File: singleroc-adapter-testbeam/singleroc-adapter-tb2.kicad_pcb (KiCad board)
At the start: 2 copper layers, 64 x 52 mm, 28 parts, among them J1 CONN_40, J2 CONN-SCSI68, P1 CONN_2

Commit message: updates to the singleroc testbeam adapter
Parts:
- C3, C4, C5, C6, C7, C8, C9: moved to B.Cu
- turned C4 to 270 degrees
- turned C5 to 270 degrees
- turned C6 to 270 degrees
- turned C7 to 270 degrees
- turned C8 to 270 degrees
- turned C9 to 270 degrees
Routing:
- net GND: track 230.6 -> 252.5 mm, vias 1 -> 0
- net AIN0: track 109.1 -> 87.5 mm
- net CTR+: track 45.7 -> 25.7 mm, vias 1 -> 2
- net CLK-: track 40.0 -> 23.2 mm, vias 1 -> 2
- net HV: track 66.5 -> 82.1 mm, vias 0 -> 1
- net VD: track 73.1 -> 59.8 mm
- net VA: track 39.9 -> 30.3 mm, vias 1 -> 2
- net TOUT-: track 54.7 -> 61.9 mm, vias 1 -> 0
- net SOUT+: track 39.1 -> 34.6 mm
- net RESET: track 43.3 -> 39.3 mm, vias 0 -> 1
- net TIN-: track 46.7 -> 43.1 mm, vias 2 -> 1
- net Net-(F1-Pad2): track 56.1 -> 52.6 mm
- net SOUT-: track 55.7 -> 53.3 mm
- net I2C_DAT+: track 65.3 -> 63.8 mm
- net I2C_A1: track 21.6 -> 20.4 mm
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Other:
- net class Default: clearance 0.126 -> 0.22; trace_width 0.254 -> 0.22
- net class pads added: clearance 0.22, trace_width 0.22, via_dia 0.889, via_drill 0.635
- rule trace_clearance: 0.126 -> 0.22
- rule trace_min: 0.254 -> 0.22
- board text added: "DESY CMS - S. Spannagel ROC Testbeam Adapter 10766-00"
- board text removed: "DESY CMS - S. Spannagel PSI46 ROC Testbeam Adapter"

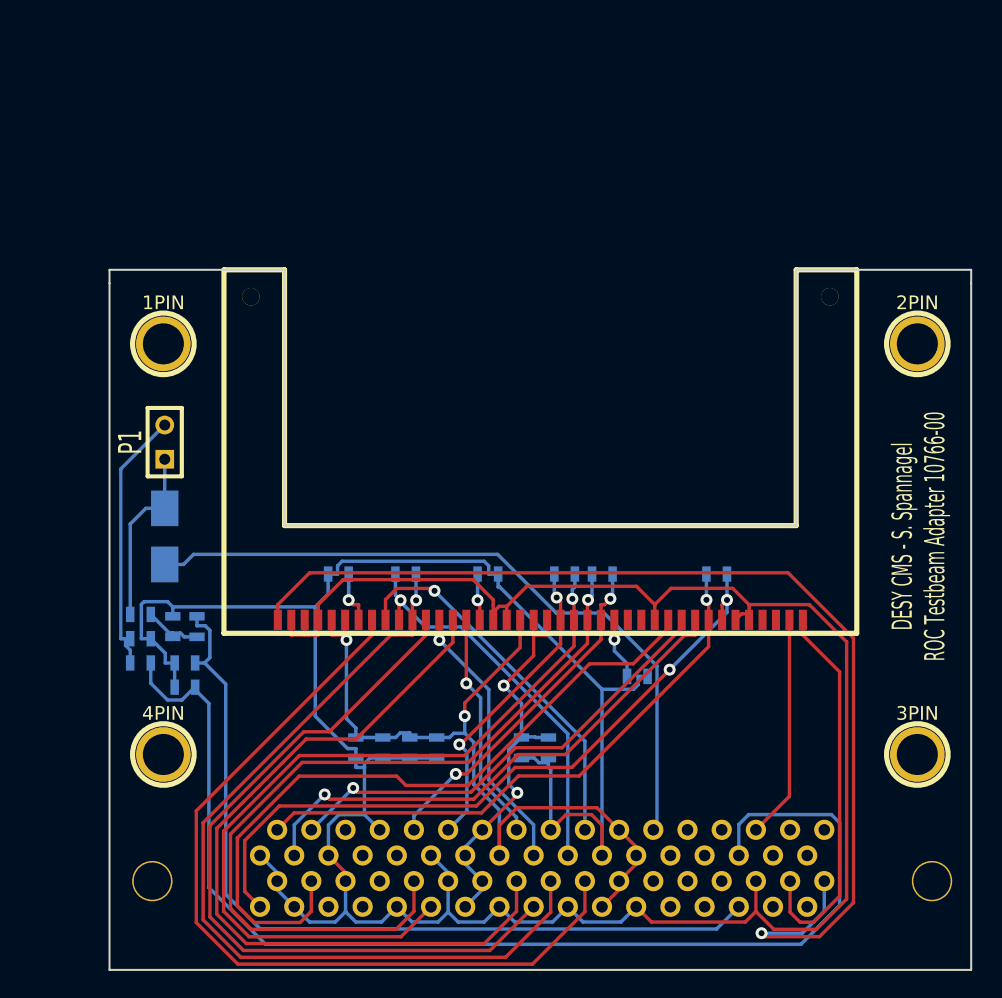
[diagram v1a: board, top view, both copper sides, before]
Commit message: More changes to Single ROC TB adapter. Sent revision 10766-01 to DESY ZE
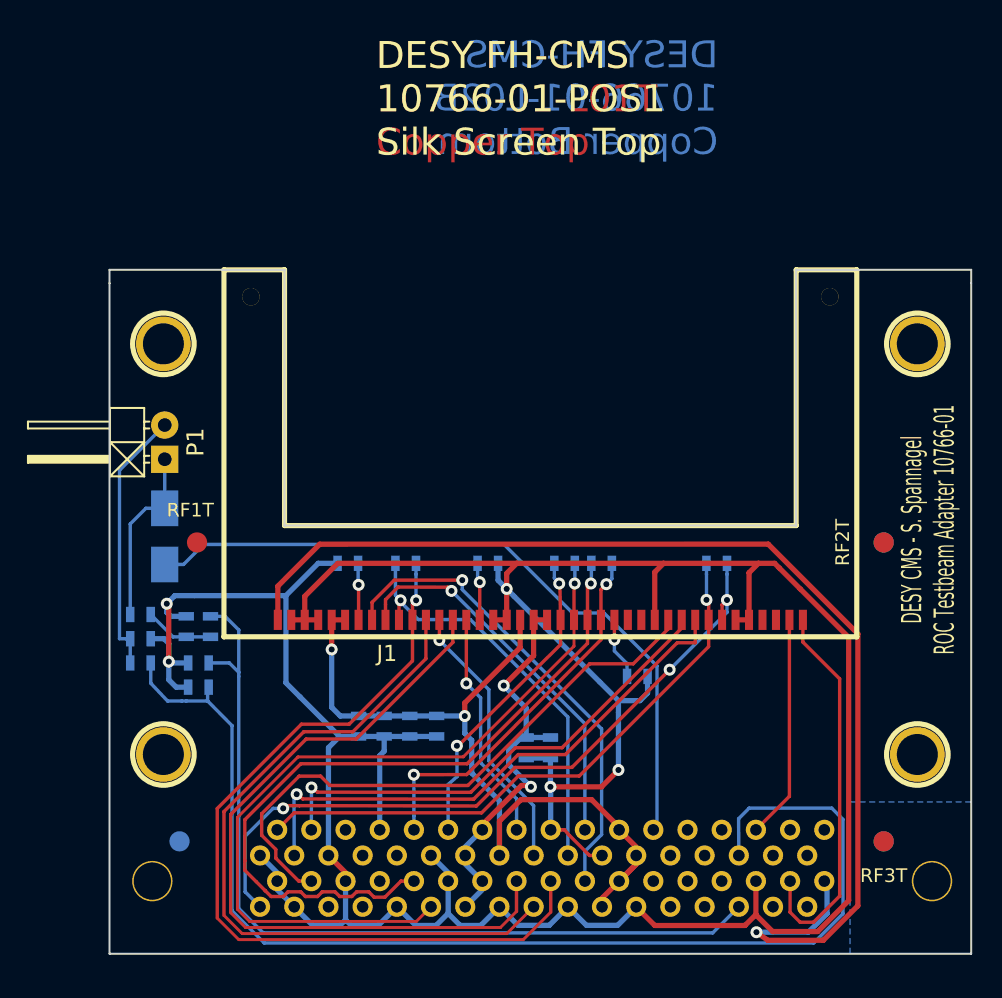
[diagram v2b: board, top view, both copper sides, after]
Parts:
- added RF1B: P***, Connect:1pin, F.Cu at (92.2, 110.5)
- added RF1T: P***, Connect:1pin, F.Cu at (93.5, 88.2)
- added RF2B, RF2T: P***, Connect:1pin, F.Cu at (144.5, 88.2)
- added RF3B, RF3T: P***, Connect:1pin, F.Cu at (144.5, 110.5)
- C1, C10, C11, C2, C3, C4, C5, C6, C7, C8, C9: footprint SMD_Packages:SM0603_Capa -> SMD0603-new:SM0603_Capa
- J1: footprint MB1:40_PIN_EDGE_CONNECTOR_MINI_CARD_BACKSIDE -> Conn40:40_PIN_EDGE_CONNECTOR_MINI_CARD_BACKSIDE
- P1: footprint Connect:SIL-2 -> Pin_Headers:Pin_Header_Angled_1x02
- R1, R2, R3, R4, R5, R6, R7, R8, R9: footprint SMD_Packages:SM0603 -> SMD0603-new:SM0603
- moved C5 1.61 mm to (105.5, 101.9)
- moved C7 1.60 mm to (107.4, 101.9)
- moved C8 1.60 mm to (109.3, 101.9)
- moved C9 1.60 mm to (111.3, 101.9)
- moved C1 1.06 mm to (104.7, 89.8)
- moved C10 1.00 mm to (93.6, 97.2)
- moved C11 1.00 mm to (93.6, 99.0)
- moved R6 1.00 mm to (94.5, 94.5)
- moved R9 1.00 mm to (92.7, 94.5)
- moved R2 0.80 mm to (123.5, 89.8)
- moved C2 0.80 mm to (115.1, 89.8)
- moved R1 0.80 mm to (109.0, 89.8)
- moved R3 0.80 mm to (120.8, 89.8)
- moved R4 0.80 mm to (132.1, 89.8)
- moved C4 0.35 mm to (118.0, 103.5)
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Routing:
- net TOUT-: track 61.9 -> 35.8 mm, vias 0 -> 1
- net SOUT-: track 53.3 -> 44.2 mm
- net HV: track 82.1 -> 87.1 mm
- net CTR-: track 60.3 -> 55.5 mm
- net I2C_A2: track 57.7 -> 55.2 mm
- net CTR+: track 25.7 -> 28.2 mm
- net SOUT+: track 34.6 -> 36.4 mm
- net CLK+: track 60.3 -> 58.5 mm
- net GND: track 252.5 -> 254.3 mm, vias 0 -> 5
- net AIN1: track 62.8 -> 64.4 mm
- net AIN0: track 87.5 -> 89.1 mm
- net RESET: track 39.3 -> 40.9 mm
- net I2C_A0: track 56.2 -> 54.7 mm
- net I2C_DAT-: track 29.2 -> 30.8 mm
- net VA: track 30.3 -> 31.4 mm
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- added copper zone on B.Cu, net (none)
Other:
- board size 64 x 52 mm -> 64 x 50.8 mm
- net class Thick added: clearance 0.391, trace_width 0.391, via_dia 0.889, via_drill 0.635
- net class pads removed
- rule pad_to_mask_clearance: 0 -> 0.07
- board text added: "DESY CMS - S. Spannagel ROC Testbeam Adapter 10766-01"
- board text added: "DESY FH-CMS 10766-01-BOHR Drill Map"
- board text added: "DESY FH-CMS 10766-01-L01T Copper Top"
- board text added: "DESY FH-CMS 10766-01-L02B Copper Bottom"
- board text added: "DESY FH-CMS 10766-01-LSM1 Solder Resist Top"
- board text added: "DESY FH-CMS 10766-01-LSM2 Solder Resist Bottom"
- board text added: "DESY FH-CMS 10766-01-POS1 Silk Screen Top"
- board text added: "DESY FH-CMS 10766-01-POS2 Silk Screen Bottom"
- board text added: "DESY FH-CMS 10766-01-SMD1 Solder Paste Top"
- board text added: "DESY FH-CMS 10766-01-SMD2 Solder Paste Bottom"
- board text removed: "DESY CMS - S. Spannagel ROC Testbeam Adapter 10766-00"

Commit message: update gerber files
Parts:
- moved RF1T 10.6 mm to (93.5, 77.7)
- moved RF2B 10.6 mm to (144.5, 77.7)
- moved RF2T 10.6 mm to (144.5, 77.7)
- moved RF1B 1.30 mm to (93.5, 110.5)
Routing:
- net GND: track 254.3 -> 263.5 mm
- net VA: track 31.4 -> 33.5 mm
- net VD: track 60.9 -> 62.5 mm
- net TIN+: track 53.7 -> 54.3 mm
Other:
- board text added: "DESY FH-CMS 10766-00-BOHR Drill Map"
- board text added: "DESY FH-CMS 10766-00-L01T Copper Top"
- board text added: "DESY FH-CMS 10766-00-L02B Copper Bottom"
- board text added: "DESY FH-CMS 10766-00-LSM1 Solder Resist Top"
- board text added: "DESY FH-CMS 10766-00-LSM2 Solder Resist Bottom"
- board text added: "DESY FH-CMS 10766-00-POS1 Silk Screen Top"
- board text added: "DESY FH-CMS 10766-00-POS2 Silk Screen Bottom"
- board text added: "DESY FH-CMS 10766-00-SMD1 Solder Paste Top"
- board text added: "DESY FH-CMS 10766-00-SMD2 Solder Paste Bottom"
- board text added: "DESY, S. Spannagel, 10766-00 CMS ROC Testbeam Adapter"
- board text removed: "DESY CMS - S. Spannagel ROC Testbeam Adapter 10766-01"
- board text removed: "DESY FH-CMS 10766-01-BOHR Drill Map"
- board text removed: "DESY FH-CMS 10766-01-L01T Copper Top"
- board text removed: "DESY FH-CMS 10766-01-L02B Copper Bottom"
- board text removed: "DESY FH-CMS 10766-01-LSM1 Solder Resist Top"
- board text removed: "DESY FH-CMS 10766-01-LSM2 Solder Resist Bottom"
- board text removed: "DESY FH-CMS 10766-01-POS1 Silk Screen Top"
- board text removed: "DESY FH-CMS 10766-01-POS2 Silk Screen Bottom"
- board text removed: "DESY FH-CMS 10766-01-SMD1 Solder Paste Top"
- board text removed: "DESY FH-CMS 10766-01-SMD2 Solder Paste Bottom"

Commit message: Add betsueckungsdruck and schematics
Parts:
- ?: renamed from 1PIN; value P*** -> (none)
- ?: renamed from 2PIN; value P*** -> (none)
- ?: renamed from 4PIN; value P*** -> (none)
- ?: renamed from 3PIN; value P*** -> (none)
- F1: value FUSE -> (none)
- J1: value CONN_40 -> (none)
- J2: value CONN-SCSI68 -> (none)
- P1: value CONN_2 -> (none)
- RF1B, RF1T, RF2B, RF2T, RF3B, RF3T: value P*** -> (none)
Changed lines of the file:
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@@
     (links 95)
     (no_connects 4)
-    (area 74.6 42.275 162.2 130.2)
+    (area 74.6 51.275 162.2 130.2)
     (thickness 1.6)
     (drawings 30)
@@
       (effects (font (size 1.5 1.2) (thickness 0.25)))
     )
-    (fp_text value CONN_40 (at 0 -28.8925) (layer B.SilkS) hide
+    (fp_text value "" (at 0 -28.8925) (layer B.SilkS) hide
       (effects (font (thickness 0.3048)) (justify mirror))
     )
@@
       (effects (font (size 1.5 1.2) (thickness 0.254)) (justify mirror))
     )
-    (fp_text value P*** (at 0 2.794) (layer F.SilkS) hide
+    (fp_text value "" (at 0 2.794) (layer F.SilkS) hide
       (effects (font (size 1.016 1.016) (thickness 0.254)))
     )
@@
       (effects (font (size 1.5 1.2) (thickness 0.254)) (justify mirror))
     )
-    (fp_text value P*** (at 0 2.794) (layer F.SilkS) hide
+    (fp_text value "" (at 0 2.794) (layer F.SilkS) hide
       (effects (font (size 1.016 1.016) (thickness 0.254)))
     )
@@
       (effects (font (size 1.5 1.2) (thickness 0.254)) (justify mirror))
     )
-    (fp_text value P*** (at 0 2.794) (layer F.SilkS) hide
+    (fp_text value "" (at 0 2.794) (layer F.SilkS) hide
       (effects (font (size 1.016 1.016) (thickness 0.254)))
     )
@@
       (effects (font (size 1.5 1.2) (thickness 0.254)))
     )
-    (fp_text value P*** (at 0 2.794) (layer F.SilkS) hide
+    (fp_text value "" (at 0 2.794) (layer F.SilkS) hide
       (effects (font (size 1.016 1.016) (thickness 0.254)))
     )
@@
       (effects (font (size 1.5 1.2) (thickness 0.254)))
     )
-    (fp_text value P*** (at 0 2.794) (layer F.SilkS) hide
+    (fp_text value "" (at 0 2.794) (layer F.SilkS) hide
       (effects (font (size 1.016 1.016) (thickness 0.254)))
     )
@@
       (effects (font (size 1.5 1.2) (thickness 0.254)))
     )
-    (fp_text value P*** (at 0 2.794) (layer F.SilkS) hide
+    (fp_text value "" (at 0 2.794) (layer F.SilkS) hide
       (effects (font (size 1.016 1.016) (thickness 0.254)))
     )
@@
       (effects (font (thickness 0.3048)) (justify mirror))
     )
-    (fp_text value FUSE (at -0.14986 -2.49936 270) (layer B.SilkS) hide
+    (fp_text value "" (at -0.14986 -2.49936 270) (layer B.SilkS) hide
       (effects (font (thickness 0.3048)) (justify mirror))
     )
@@
       (effects (font (size 1.5 1.2) (thickness 0.25)) (justify mirror))
     )
-    (fp_text value CONN-SCSI68 (at 0 7.62 180) (layer B.SilkS) hide
+    (fp_text value "" (at 0.05 -12.15 180) (layer B.SilkS) hide
       (effects (font (size 1 1) (thickness 0.15)) (justify mirror))
     )
@@
     (descr "module 1 pin (ou trou mecanique de percage)")
     (tags DEV)
-    (fp_text reference 1PIN (at 0 -3.048) (layer F.SilkS) hide
-      (effects (font (size 1.016 1.016) (thickness 0.254)))
-    )
-    (fp_text value P*** (at 0 2.794) (layer F.SilkS) hide
+    (fp_text reference "" (at 0 -3.048) (layer F.SilkS) hide
+      (effects (font (size 1.016 1.016) (thickness 0.254)))
+    )
+    (fp_text value "" (at 0 2.794) (layer F.SilkS) hide
       (effects (font (size 1.016 1.016) (thickness 0.254)))
     )
@@
     (descr "module 1 pin (ou trou mecanique de percage)")
     (tags DEV)
-    (fp_text reference 2PIN (at 0 -3.048) (layer F.SilkS) hide
-      (effects (font (size 1.016 1.016) (thickness 0.254)))
-    )
-    (fp_text value P*** (at 0 2.794) (layer F.SilkS) hide
+    (fp_text reference "" (at 0 -3.048) (layer F.SilkS) hide
+      (effects (font (size 1.016 1.016) (thickness 0.254)))
+    )
+    (fp_text value "" (at 0 2.794) (layer F.SilkS) hide
       (effects (font (size 1.016 1.016) (thickness 0.254)))
     )
@@
     (descr "module 1 pin (ou trou mecanique de percage)")
     (tags DEV)
-    (fp_text reference 4PIN (at 0 -3.048) (layer F.SilkS) hide
-      (effects (font (size 1.016 1.016) (thickness 0.254)))
-    )
-    (fp_text value P*** (at 0 2.794) (layer F.SilkS) hide
+    (fp_text reference "" (at 0 -3.048) (layer F.SilkS) hide
+      (effects (font (size 1.016 1.016) (thickness 0.254)))
+    )
+    (fp_text value "" (at 0 2.794) (layer F.SilkS) hide
       (effects (font (size 1.016 1.016) (thickness 0.254)))
     )
@@
     (descr "module 1 pin (ou trou mecanique de percage)")
     (tags DEV)
-    (fp_text reference 3PIN (at 0 -3.048) (layer F.SilkS) hide
-      (effects (font (size 1.016 1.016) (thickness 0.254)))
-    )
-    (fp_text value P*** (at 0 2.794) (layer F.SilkS) hide
+    (fp_text reference "" (at 0 -3.048) (layer F.SilkS) hide
+      (effects (font (size 1.016 1.016) (thickness 0.254)))
+    )
+    (fp_text value "" (at 0 2.794) (layer F.SilkS) hide
       (effects (font (size 1.016 1.016) (thickness 0.254)))
     )
@@
       (effects (font (size 1.2 1) (thickness 0.25)) (justify mirror))
     )
-    (fp_text value 100nF (at 1.85 0 270) (layer B.SilkS) hide
+    (fp_text value 100nF (at -1.85 0 270) (layer B.SilkS) hide
       (effects (font (size 0.508 0.4572) (thickness 0.1143)) (justify mirror))
     )
@@
       (effects (font (size 1.2 1) (thickness 0.25)) (justify mirror))
     )
-    (fp_text value 100nF (at 1.85 0 270) (layer B.SilkS) hide
+    (fp_text value 100nF (at -1.85 0.05 270) (layer B.SilkS) hide
       (effects (font (size 0.508 0.4572) (thickness 0.1143)) (justify mirror))
     )
@@
       (effects (font (size 1.27 1.27) (thickness 0.2032)))
     )
-    (fp_text value CONN_2 (at 0 0 90) (layer F.SilkS) hide
+    (fp_text value "" (at 0 0 90) (layer F.SilkS) hide
       (effects (font (size 1.27 1.27) (thickness 0.2032)))
     )

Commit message: Update REF markers: pads&footprint on the correct side of the board (was flipped somehow, footprint on wrong side, pad on correct one), update PICK&PLACE file to include REF markers.
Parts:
- RF1B, RF2B, RF3B: moved to B.Cu
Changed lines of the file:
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@@
-(kicad_pcb (version 4) (host pcbnew "(2014-10-13 BZR 5186)-product")
+(kicad_pcb (version 4) (host pcbnew "(2014-11-30 BZR 5308)-product")
   (general
     (links 95)
@@
     (mod_text_size 1 1)
     (mod_text_width 0.15)
-    (pad_size 1.30048 1.30048)
-    (pad_drill 1.30048)
+    (pad_size 1.5 1.5)
+    (pad_drill 0)
     (pad_to_mask_clearance 0.07)
     (solder_mask_min_width 0.07)
@@
       (net 13 HV))
   )
-  (module Connect:1pin (layer F.Cu)
+  (module Connect:1pin (layer B.Cu)
     (at 93.5 110.5)
     (descr "module 1 pin (ou trou mecanique de percage)")
     (tags DEV)
+    (attr smd)
     (fp_text reference RF1B (at -3.35 0) (layer B.SilkS)
       (effects (font (size 1.5 1.2) (thickness 0.254)) (justify mirror))
     )
+    (fp_text value "" (at 0 -2.794) (layer B.SilkS) hide
+      (effects (font (size 1.016 1.016) (thickness 0.254)) (justify mirror))
+    )
+    (pad 1 smd circle (at 0 0) (size 1.5 1.5) (layers B.Cu F.Paste F.Mask)
+      (solder_mask_margin 0.75))
+  )
+  (module Connect:1pin (layer B.Cu)
+    (at 144.5 110.45)
+    (descr "module 1 pin (ou trou mecanique de percage)")
+    (tags DEV)
+    (attr smd)
+    (fp_text reference RF3B (at -0.3 2.35) (layer B.SilkS)
+      (effects (font (size 1.5 1.2) (thickness 0.254)) (justify mirror))
+    )
+    (fp_text value "" (at 0 -2.794) (layer B.SilkS) hide
+      (effects (font (size 1.016 1.016) (thickness 0.254)) (justify mirror))
+    )
+    (pad 1 smd circle (at 0 0) (size 1.5 1.5) (layers B.Cu F.Paste F.Mask)
+      (solder_mask_margin 0.75))
+  )
+  (module Connect:1pin (layer B.Cu)
+    (at 144.5 77.65)
+    (descr "module 1 pin (ou trou mecanique de percage)")
+    (tags DEV)
+    (attr smd)
+    (fp_text reference RF2B (at -3.1 0 90) (layer B.SilkS)
+      (effects (font (size 1.5 1.2) (thickness 0.254)) (justify mirror))
+    )
+    (fp_text value "" (at 0 -2.794) (layer B.SilkS) hide
+      (effects (font (size 1.016 1.016) (thickness 0.254)) (justify mirror))
+    )
+    (pad 1 smd circle (at 0 0) (size 1.5 1.5) (layers B.Cu F.Paste F.Mask)
+      (solder_mask_margin 0.75))
+  )
+  (module Connect:1pin (layer F.Cu)
+    (at 144.5 110.45)
+    (descr "module 1 pin (ou trou mecanique de percage)")
+    (tags DEV)
+    (attr smd)
+    (fp_text reference RF3T (at -0.3 2.35) (layer F.SilkS)
+      (effects (font (size 1.5 1.2) (thickness 0.254)))
+    )
     (fp_text value "" (at 0 2.794) (layer F.SilkS) hide
       (effects (font (size 1.016 1.016) (thickness 0.254)))
     )
-    (pad 1 smd circle (at 0 0) (size 1.5 1.5) (layers B.Cu B.Paste B.Mask)
+    (pad 1 smd circle (at 0 0) (size 1.5 1.5) (layers F.Cu F.Paste F.Mask)
       (solder_mask_margin 0.75))
   )
   (module Connect:1pin (layer F.Cu)
-    (at 144.5 110.45)
-    (descr "module 1 pin (ou trou mecanique de percage)")
-    (tags DEV)
-    (fp_text reference RF3B (at -0.25 2.35) (layer B.SilkS)
-      (effects (font (size 1.5 1.2) (thickness 0.254)) (justify mirror))
+    (at 144.5 77.65)
+    (descr "module 1 pin (ou trou mecanique de percage)")
+    (tags DEV)
+    (attr smd)
+    (fp_text reference RF2T (at -3.1 0 90) (layer F.SilkS)
+      (effects (font (size 1.5 1.2) (thickness 0.254)))
     )
     (fp_text value "" (at 0 2.794) (layer F.SilkS) hide
       (effects (font (size 1.016 1.016) (thickness 0.254)))
     )
-    (pad 1 smd circle (at 0 0) (size 1.5 1.5) (layers B.Cu B.Paste B.Mask)
-      (solder_mask_margin 0.75))
-  )
-  (module Connect:1pin (layer F.Cu)
-    (at 144.5 77.65)
-    (descr "module 1 pin (ou trou mecanique de percage)")
-    (tags DEV)
-    (fp_text reference RF2B (at -3.1 0 90) (layer B.SilkS)
-      (effects (font (size 1.5 1.2) (thickness 0.254)) (justify mirror))
-    )
-    (fp_text value "" (at 0 2.794) (layer F.SilkS) hide
-      (effects (font (size 1.016 1.016) (thickness 0.254)))
-    )
-    (pad 1 smd circle (at 0 0) (size 1.5 1.5) (layers B.Cu B.Paste B.Mask)
-      (solder_mask_margin 0.75))
-  )
-  (module Connect:1pin (layer F.Cu)
-    (at 144.5 110.45)
-    (descr "module 1 pin (ou trou mecanique de percage)")
-    (tags DEV)
-    (fp_text reference RF3T (at -0.3 2.35) (layer F.SilkS)
-      (effects (font (size 1.5 1.2) (thickness 0.254)))
-    )
-    (fp_text value "" (at 0 2.794) (layer F.SilkS) hide
-      (effects (font (size 1.016 1.016) (thickness 0.254)))
-    )
     (pad 1 smd circle (at 0 0) (size 1.5 1.5) (layers F.Cu F.Paste F.Mask)
       (solder_mask_margin 0.75))
   )
   (module Connect:1pin (layer F.Cu)
-    (at 144.5 77.65)
-    (descr "module 1 pin (ou trou mecanique de percage)")
-    (tags DEV)
-    (fp_text reference RF2T (at -3.1 0 90) (layer F.SilkS)
-      (effects (font (size 1.5 1.2) (thickness 0.254)))
-    )
-    (fp_text value "" (at 0 2.794) (layer F.SilkS) hide
-      (effects (font (size 1.016 1.016) (thickness 0.254)))
-    )
-    (pad 1 smd circle (at 0 0) (size 1.5 1.5) (layers F.Cu F.Paste F.Mask)
-      (solder_mask_margin 0.75))
-  )
-  (module Connect:1pin (layer F.Cu)
     (at 93.5 77.65)
     (descr "module 1 pin (ou trou mecanique de percage)")
     (tags DEV)
     (solder_mask_margin 3)
+    (attr smd)
     (fp_text reference RF1T (at 3.25 0 90) (layer F.SilkS)
       (effects (font (size 1.5 1.2) (thickness 0.254)))
